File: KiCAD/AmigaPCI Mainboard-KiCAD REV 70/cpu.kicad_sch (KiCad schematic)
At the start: 56 parts, among them CN200 DIN41612_03x50, CN712 SPI, J712_TP0 U712_TP, U216 74LVC244, U712 ICE40HX4K-TQ144, U712F1 W25X20CLSN

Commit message: Add JLCPCB part numbers and fix 74LVC244 footprints.
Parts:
- C255, C719, C720, C721, C722, C723, C724, C725, C726, C727, C728, C730, C736: LCSC (none) -> C14663
- C729, C735: LCSC (none) -> C96446
- CN712: LCSC (none) -> C37208
- J712_TP0: LCSC (none) -> C81276
- R218, R251, R252, R253: LCSC (none) -> C25254
- R219, R271: LCSC (none) -> C23345
- R221, R234, R235, R236, R242, R243, R244, R245, R246, R276, R277, R278: LCSC (none) -> C13167
- R280, R281: LCSC (none) -> C4190
- R288, R289: LCSC (none) -> C21190
- R700, R701: LCSC (none) -> C22775
- R702, R703: LCSC (none) -> C25804
- RN200, RN201, RN202, RN203, RN204, RN205, RN206, RN207, RN209: LCSC (none) -> C1731077
- U216: footprint Package_SO:SSOP-20_4.4x6.5mm_P0.65mm -> Package_SO:TSSOP-20_4.4x6.5mm_P0.65mm; LCSC (none) -> C7668
- U712: LCSC (none) -> C1521989
- U712F1: LCSC (none) -> C34591

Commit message: Add part number for DIN41612 connector.
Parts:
- CN200: LCSC (none) -> C3646680
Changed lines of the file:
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@@
 			)
 		)
-		(property "LCSC" ""
+		(property "LCSC" "C3646680"
 			(at 234.95 147.32 0)
 			(effects

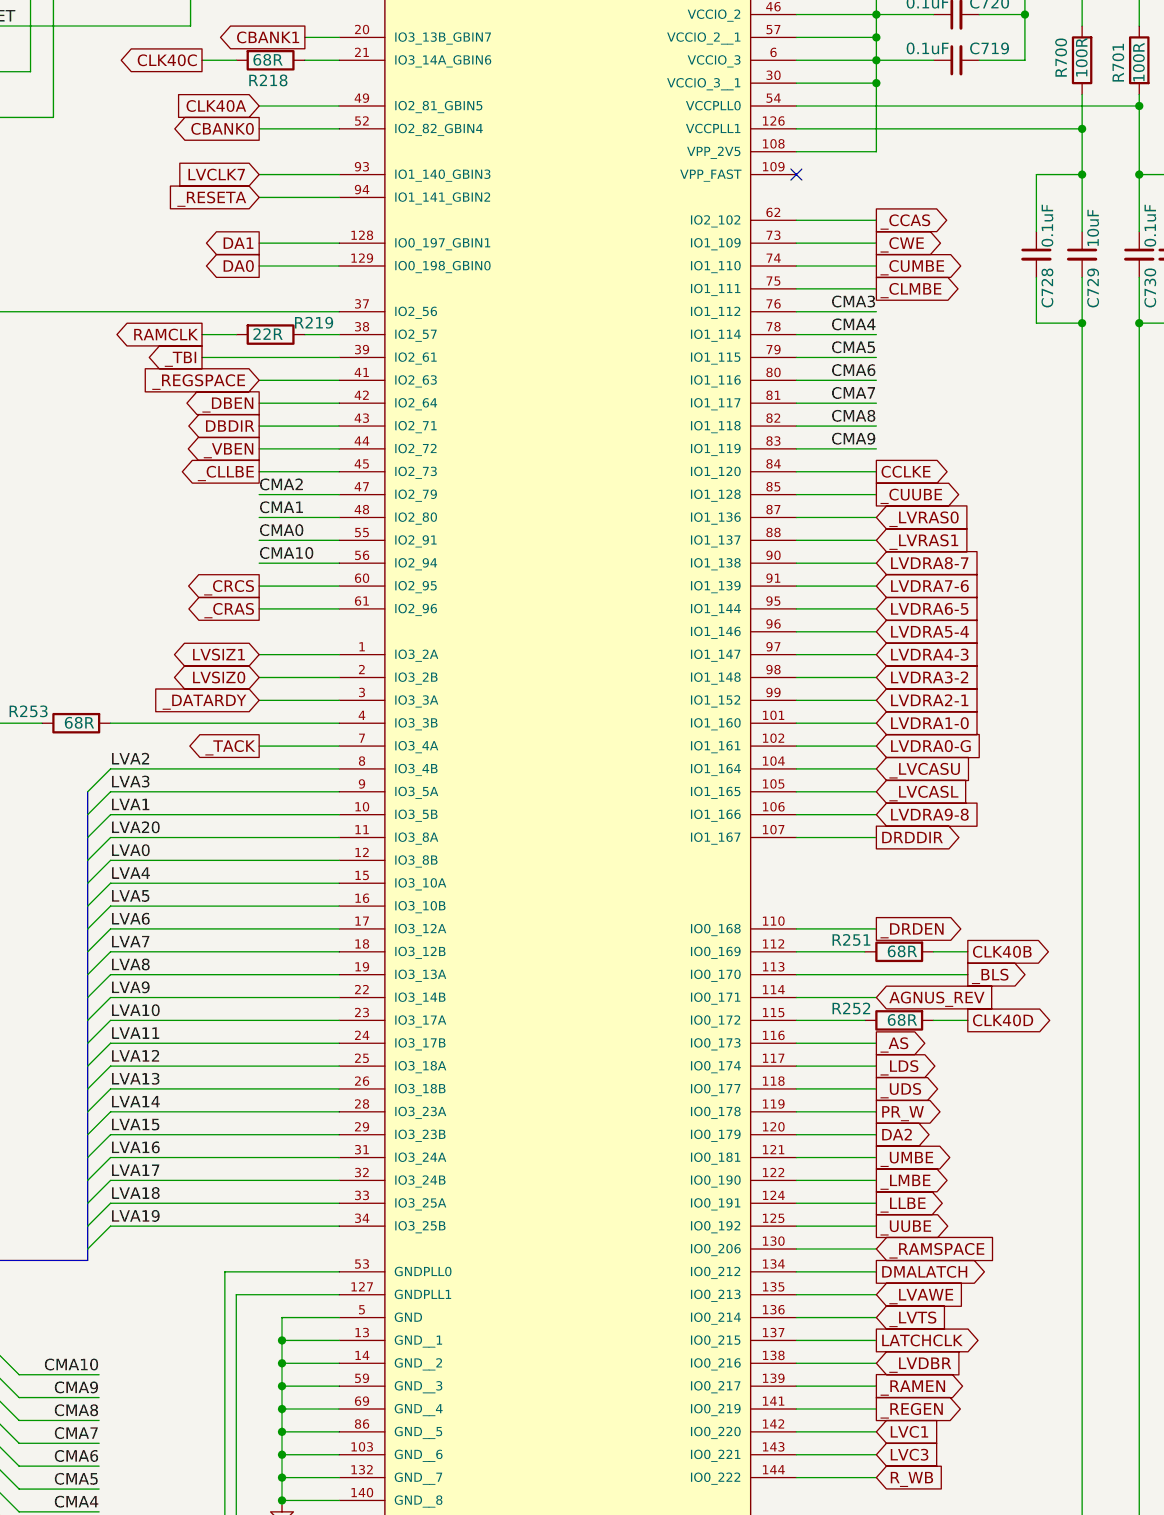
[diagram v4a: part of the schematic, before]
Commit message: Updates to revision 7 board.
Change U810 to 74LVC245 buffers
Add CDAC to U712
Add address latch to CIAs
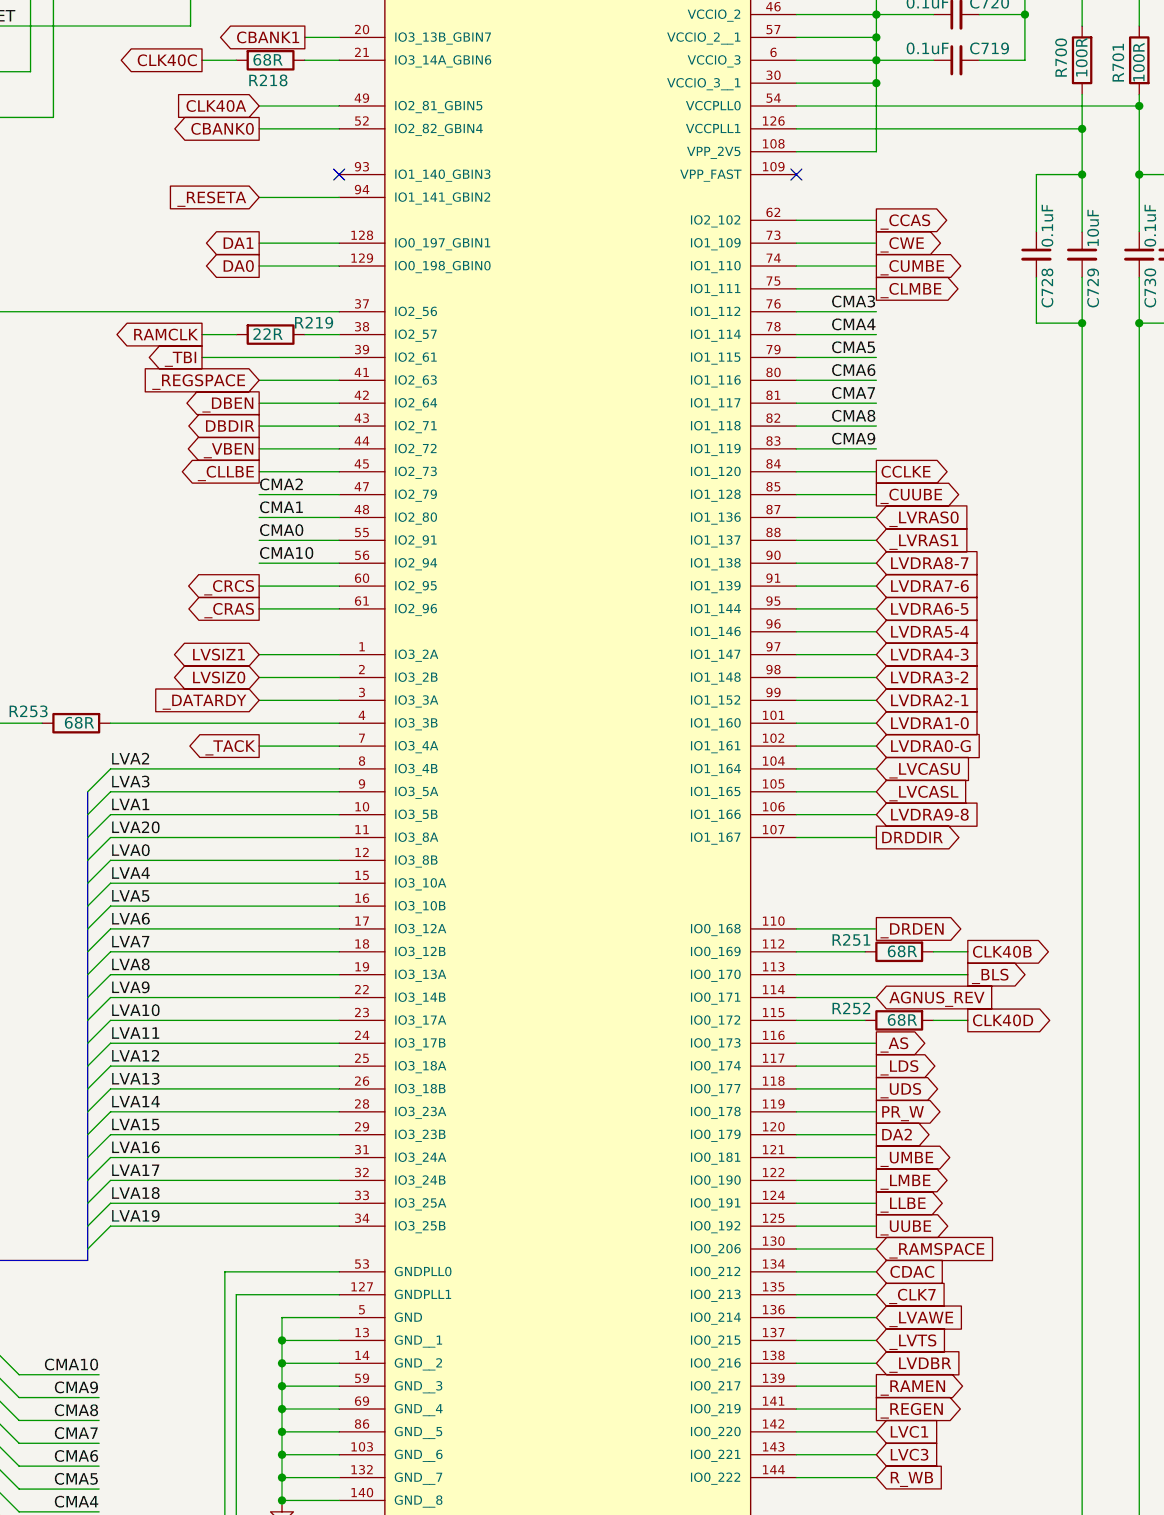
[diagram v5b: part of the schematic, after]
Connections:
- net LATCHCLK is gone; now on net _LVTS: U712.137 (IO0_215)
- net _LVAWE: now also U712.136 (IO0_214); no longer U712.135 (IO0_213)
- net _LVTS: no longer U712.136 (IO0_214)
- net DMALATCH renamed CDAC
- net LVCLK7: no longer names the net of U712.93 (IO1_140_GBIN3)
- new net _CLK7: U712.135 (IO0_213)
- no-connect marks 27 -> 28
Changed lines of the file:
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@@
 	(title_block
 		(title "AMIGA PCI")
-		(date "2026-04-27")
+		(date "2026-06-06")
 		(rev "7.0")
 	)
@@
 	)
 	(no_connect
+		(at 77.47 83.82)
+	)
+	(no_connect
 		(at 128.27 83.82)
 	)
@@
 	(wire
 		(pts
-			(xy 77.47 83.82) (xy 68.58 83.82)
-		)
-		(stroke
-			(width 0)
-			(type default)
-		)
-	)
-	(wire
-		(pts
 			(xy 137.16 134.62) (xy 128.27 134.62)
 		)
@@
 		)
 	)
-	(global_label "LATCHCLK"
-		(shape output)
-		(at 137.16 213.36 0)
-		(fields_autoplaced yes)
-		(effects
-			(font
-				(size 1.27 1.27)
-			)
-			(justify left)
-		)
-		(property "Intersheetrefs" "${INTERSHEET_REFS}"
-			(at 149.3981 213.36 0)
-			(effects
-				(font
-					(size 1.27 1.27)
-				)
-				(justify left)
-			)
-		)
-	)
-	(global_label "DMALATCH"
-		(shape output)
-		(at 137.16 205.74 0)
-		(fields_autoplaced yes)
-		(effects
-			(font
-				(size 1.27 1.27)
-			)
-			(justify left)
-		)
-		(property "Intersheetrefs" "${INTERSHEET_REFS}"
-			(at 149.64 205.74 0)
-			(effects
-				(font
-					(size 1.27 1.27)
-				)
-				(justify left)
-			)
-		)
-	)
 	(global_label "_CPURST"
 		(shape input)
@@
 		)
 	)
-	(global_label "LVCLK7"
+	(global_label "_CLK7"
 		(shape input)
-		(at 68.58 83.82 180)
+		(at 137.16 208.28 0)
 		(fields_autoplaced yes)
 		(effects
@@
 				(size 1.27 1.27)
 			)
-			(justify right)
+			(justify left)
 		)
 		(property "Intersheetrefs" "${INTERSHEET_REFS}"
-			(at 58.7005 83.82 0)
+			(at 145.8904 208.28 0)
 			(effects
 				(font
 					(size 1.27 1.27)
 				)
-				(justify right)
+				(justify left)
 			)
 		)
@@
 	(global_label "_LVAWE"
 		(shape input)
-		(at 137.16 208.28 0)
+		(at 137.16 210.82 0)
 		(fields_autoplaced yes)
 		(effects
@@
 		)
 		(property "Intersheetrefs" "${INTERSHEET_REFS}"
-			(at 147.1132 208.28 0)
+			(at 147.1132 210.82 0)
 			(effects
 				(font
@@
 		)
 	)
+	(global_label "CDAC"
+		(shape input)
+		(at 137.16 205.74 0)
+		(fields_autoplaced yes)
+		(effects
+			(font
+				(size 1.2954 1.2954)
+			)
+			(justify left)
+		)
+		(property "Intersheetrefs" "${INTERSHEET_REFS}"
+			(at 145.2009 205.74 0)
+			(effects
+				(font
+					(size 1.27 1.27)
+				)
+				(justify left)
+			)
+		)
+	)
 	(global_label "CLK40A"
 		(shape output)
@@
 	(global_label "_LVTS"
 		(shape input)
-		(at 137.16 210.82 0)
+		(at 137.16 213.36 0)
 		(fields_autoplaced yes)
 		(effects
@@
 		)
 		(property "Intersheetrefs" "${INTERSHEET_REFS}"
-			(at 145.5711 210.82 0)
+			(at 145.5711 213.36 0)
 			(effects
 				(font
